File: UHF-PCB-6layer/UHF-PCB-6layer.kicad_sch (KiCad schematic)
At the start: 21 parts, among them IC1 MC100EL1648DG, U1 MAC-24+, U2 LTC1566-1IS8-PBF, U3 TAV1-331+, U5 XMSM0G3507SPT, U6 XC7A100T-CSG324_A

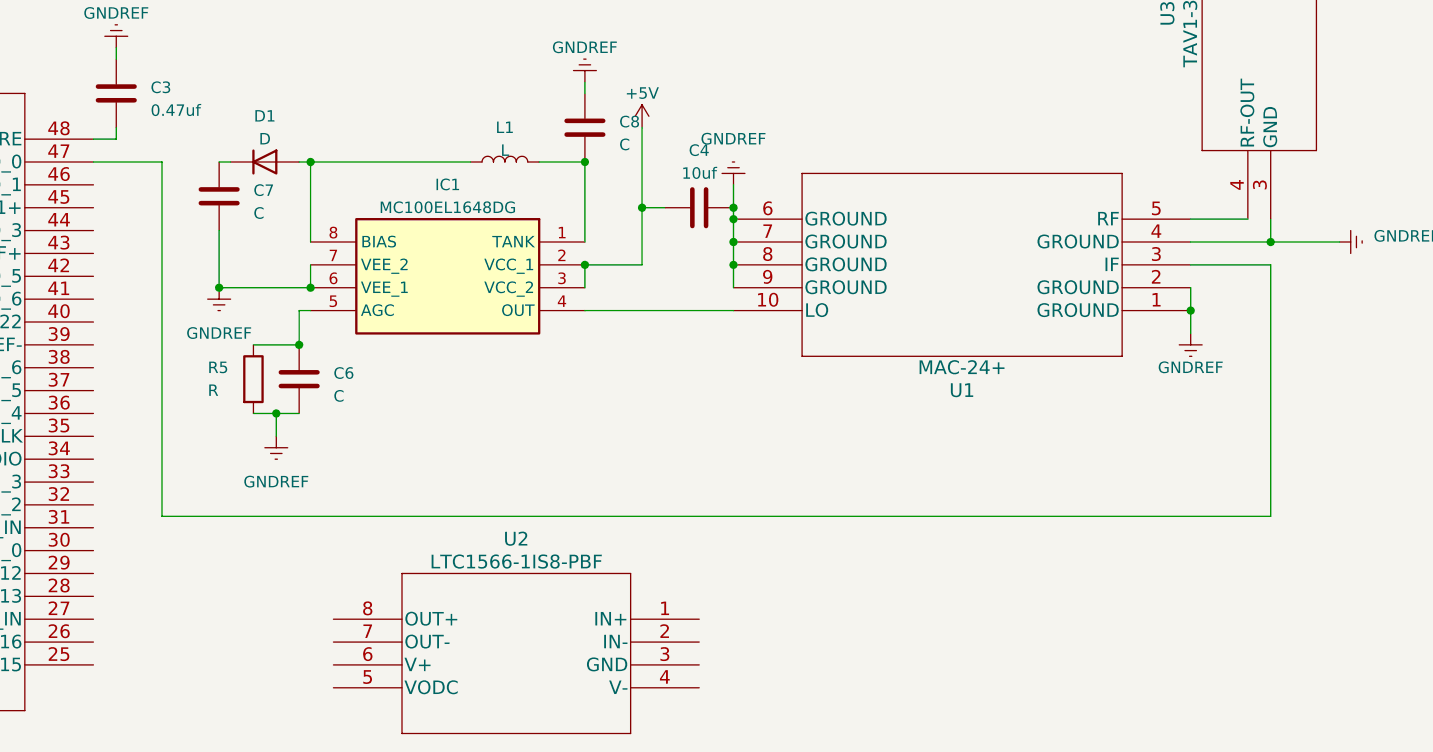
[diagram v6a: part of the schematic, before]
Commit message: added 2.3MHz LPF to input of module
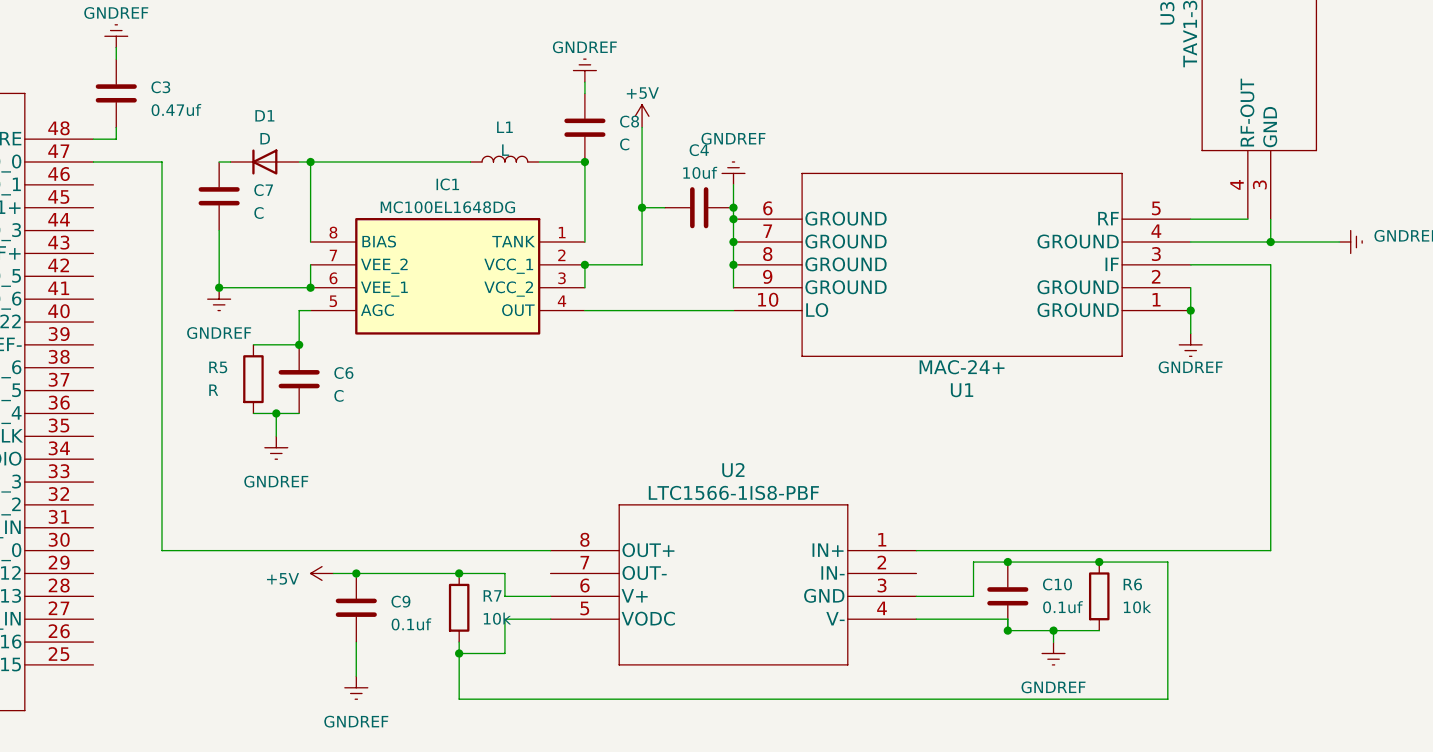
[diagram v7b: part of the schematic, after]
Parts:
- added C10, C9: 0.1uf, Capacitor_SMD:C_0603_1608Metric, symbol Device:C
- added R6, R7: 10k, Resistor_SMD:R_0603_1608Metric, symbol Device:R
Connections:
- net +5V: now also U2.6 (V+), C9.1, R7.1
- net GNDREF: now also U2.4 (V-), C10.2, C9.2, R6.2
- net at U1.3 (IF): now also U2.1 (IN+); no longer U5.47 (PA27_/_RTC_OUT_/_A0_0)
- net at U2.3 (GND): now also U2.5 (VODC), C10.1, R6.1, R7.2
- net at U2.8 (OUT+): now also U5.47 (PA27_/_RTC_OUT_/_A0_0)
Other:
- moved on the sheet: U2

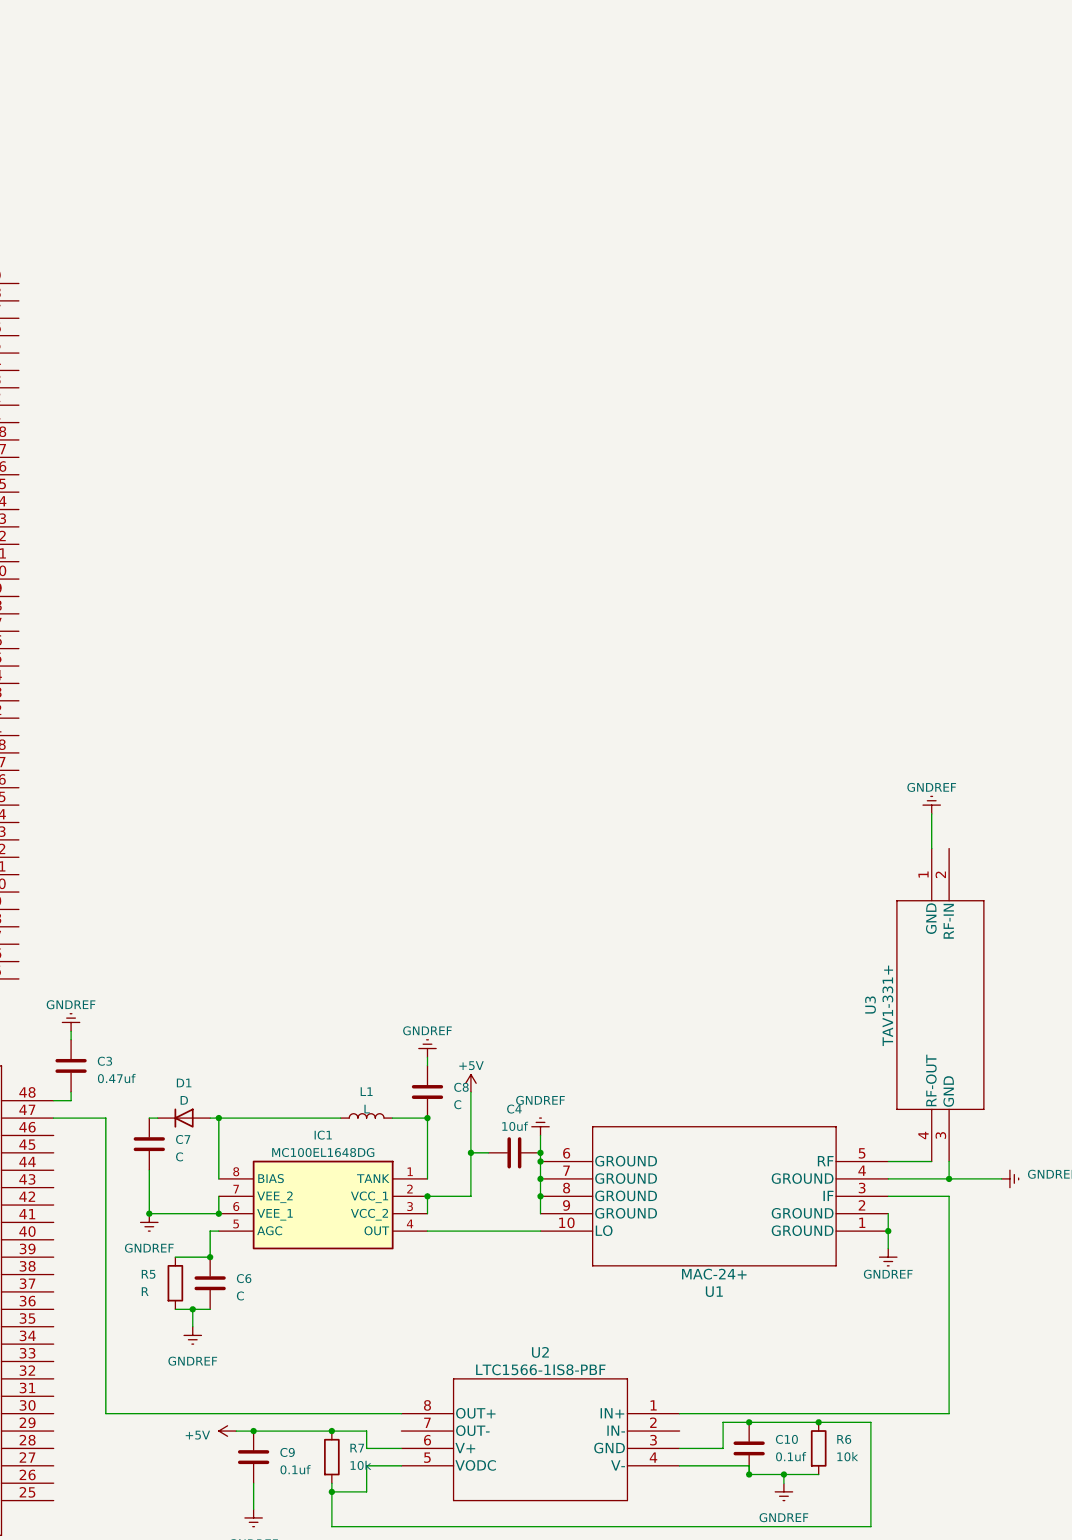
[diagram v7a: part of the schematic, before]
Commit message: added connector for power, 3.3v, 5v, gnd, and IF signal
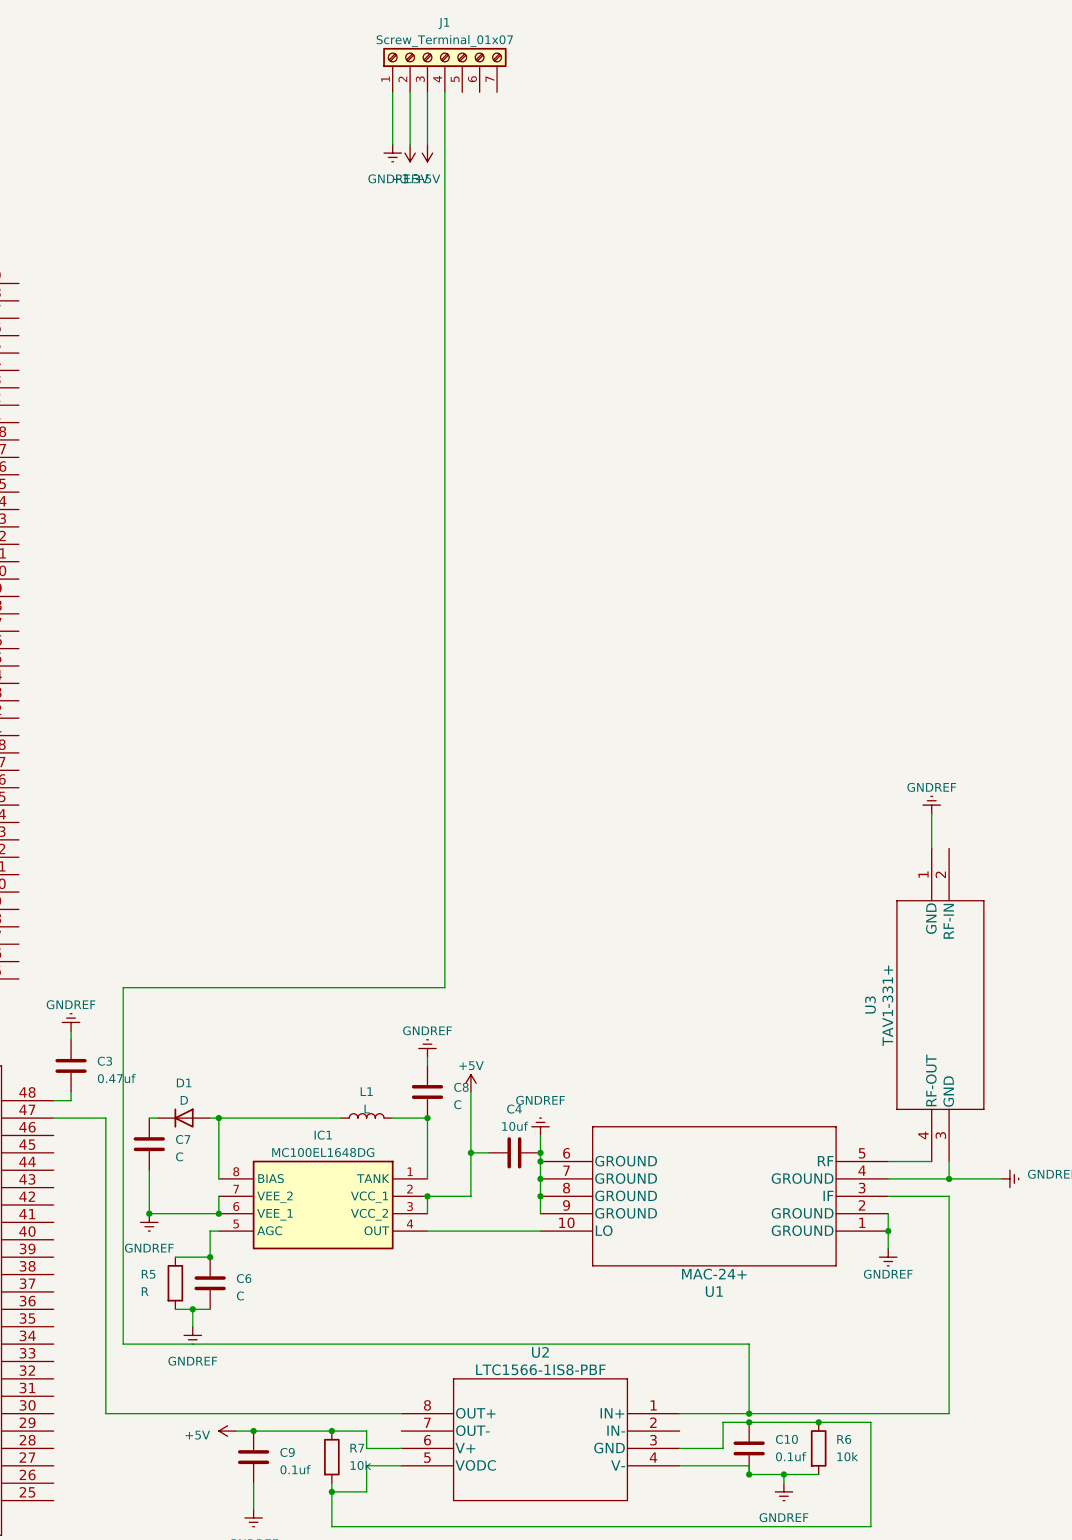
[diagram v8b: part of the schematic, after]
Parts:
- added J1: Screw_Terminal_01x07, TerminalBlock_Altech:Altech_AK300_1x07_P5.00mm_45-Degree, symbol Connector:Screw_Terminal_01x07
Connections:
- net +3.3V: now also J1.2 (Pin_2)
- net +5V: now also J1.3 (Pin_3)
- net GNDREF: now also J1.1 (Pin_1)
- net at U1.3 (IF), U2.1 (IN+): now also J1.4 (Pin_4)
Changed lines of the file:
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@@
   (junction (at 101.6 189.23) (diameter 0) (color 0 0 0 0)
   )
+  (junction (at 346.71 217.17) (diameter 0) (color 0 0 0 0)
+  )
   (junction (at 375.92 182.88) (diameter 0) (color 0 0 0 0)
   )
@@
     (stroke (width 0) (type default))
   )
+  (wire (pts (xy 302.26 154.94) (xy 255.27 154.94))
+    (stroke (width 0) (type default))
+  )
   (wire (pts (xy 101.6 193.04) (xy 101.6 195.58))
     (stroke (width 0) (type default))
@@
     (stroke (width 0) (type default))
   )
+  (wire (pts (xy 346.71 207.01) (xy 346.71 217.17))
+    (stroke (width 0) (type default))
+  )
   (wire (pts (xy 383.54 182.88) (xy 375.92 182.88))
     (stroke (width 0) (type default))
@@
     (stroke (width 0) (type default))
   )
+  (wire (pts (xy 299.72 24.13) (xy 299.72 31.75))
+    (stroke (width 0) (type default))
+  )
   (wire (pts (xy 308.61 179.07) (xy 306.07 179.07))
     (stroke (width 0) (type default))
@@
     (stroke (width 0) (type default))
   )
-  (wire (pts (xy 336.55 217.17) (xy 375.92 217.17))
+  (wire (pts (xy 336.55 217.17) (xy 346.71 217.17))
     (stroke (width 0) (type default))
   )
@@
     (stroke (width 0) (type default))
   )
+  (wire (pts (xy 294.64 24.13) (xy 294.64 31.75))
+    (stroke (width 0) (type default))
+  )
   (wire (pts (xy 364.49 218.44) (xy 364.49 233.68))
     (stroke (width 0) (type default))
@@
     (stroke (width 0) (type default))
   )
+  (wire (pts (xy 255.27 207.01) (xy 346.71 207.01))
+    (stroke (width 0) (type default))
+  )
+  (wire (pts (xy 255.27 154.94) (xy 255.27 207.01))
+    (stroke (width 0) (type default))
+  )
   (wire (pts (xy 118.11 173.99) (xy 123.19 173.99))
     (stroke (width 0) (type default))
   )
+  (wire (pts (xy 302.26 24.13) (xy 302.26 154.94))
+    (stroke (width 0) (type default))
+  )
   (wire (pts (xy 259.08 181.61) (xy 259.08 187.96))
     (stroke (width 0) (type default))
@@
     (stroke (width 0) (type default))
   )
+  (wire (pts (xy 346.71 217.17) (xy 375.92 217.17))
+    (stroke (width 0) (type default))
+  )
   (wire (pts (xy 123.19 173.99) (xy 123.19 167.64))
     (stroke (width 0) (type default))
@@
     (stroke (width 0) (type default))
   )
+  (wire (pts (xy 297.18 24.13) (xy 297.18 31.75))
+    (stroke (width 0) (type default))
+  )
   (wire (pts (xy 295.91 224.79) (xy 290.83 224.79))
     (stroke (width 0) (type default))
@@
         (path "/408f5dbf-8c57-4b84-b0cc-1d788fcf6d08"
           (reference "L1") (unit 1)
+        )
+      )
+    )
+  )
+  (symbol (lib_id "Connector:Screw_Terminal_01x07") (at 302.26 19.05 90) (unit 1)
+    (in_bom yes) (on_board yes) (dnp no) (fields_autoplaced)
+    (property "Reference" "J1" (at 302.26 13.97 90)
+      (effects (font (size 1.27 1.27)))
+    )
+    (property "Value" "Screw_Terminal_01x07" (at 302.26 16.51 90)
+      (effects (font (size 1.27 1.27)))
+    )
+    (property "Footprint" "TerminalBlock_Altech:Altech_AK300_1x07_P5.00mm_45-Degree" (at 302.26 19.05 0)
+      (effects (font (size 1.27 1.27)) hide)
+    )
+    (property "Datasheet" "~" (at 302.26 19.05 0)
+      (effects (font (size 1.27 1.27)) hide)
+    )
+    (pin "1")
+    (pin "2")
+    (pin "3")
+    (pin "4")
+    (pin "5")
+    (pin "6")
+    (pin "7")
+    (instances
+      (project "UHF-PCB-6layer"
+        (path "/408f5dbf-8c57-4b84-b0cc-1d788fcf6d08"
+          (reference "J1") (unit 1)
         )
       )
@@
         (path "/408f5dbf-8c57-4b84-b0cc-1d788fcf6d08"
           (reference "U1") (unit 1)
+        )
+      )
+    )
+  )
+  (symbol (lib_id "power:+5V") (at 299.72 31.75 180) (unit 1)
+    (in_bom yes) (on_board yes) (dnp no) (fields_autoplaced)
+    (property "Reference" "#PWR018" (at 299.72 27.94 0)
+      (effects (font (size 1.27 1.27)) hide)
+    )
+    (property "Value" "+5V" (at 299.72 36.83 0)
+      (effects (font (size 1.27 1.27)))
+    )
+    (property "Footprint" "" (at 299.72 31.75 0)
+      (effects (font (size 1.27 1.27)) hide)
+    )
+    (property "Datasheet" "" (at 299.72 31.75 0)
+      (effects (font (size 1.27 1.27)) hide)
+    )
+    (pin "1")
+    (instances
+      (project "UHF-PCB-6layer"
+        (path "/408f5dbf-8c57-4b84-b0cc-1d788fcf6d08"
+          (reference "#PWR018") (unit 1)
         )
       )
@@
         )
       )
+    )
+  )
+  (symbol (lib_id "power:GNDREF") (at 294.64 31.75 0) (unit 1)
+    (in_bom yes) (on_board yes) (dnp no) (fields_autoplaced)
+    (property "Reference" "#PWR017" (at 294.64 38.1 0)
+      (effects (font (size 1.27 1.27)) hide)
+    )
+    (property "Value" "GNDREF" (at 294.64 36.83 0)
+      (effects (font (size 1.27 1.27)))
+    )
+    (property "Footprint" "" (at 294.64 31.75 0)
+      (effects (font (size 1.27 1.27)) hide)
+    )
+    (property "Datasheet" "" (at 294.64 31.75 0)
+      (effects (font (size 1.27 1.27)) hide)
+    )
+    (pin "1")
+    (instances
+      (project "UHF-PCB-6layer"
+        (path "/408f5dbf-8c57-4b84-b0cc-1d788fcf6d08"
+          (reference "#PWR017") (unit 1)
+        )
+      )
+    )
+  )
+  (symbol (lib_id "power:+3.3V") (at 297.18 31.75 180) (unit 1)
+    (in_bom yes) (on_board yes) (dnp no) (fields_autoplaced)
+    (property "Reference" "#PWR019" (at 297.18 27.94 0)
+      (effects (font (size 1.27 1.27)) hide)
+    )
+    (property "Value" "+3.3V" (at 297.18 36.83 0)
+      (effects (font (size 1.27 1.27)))
+    )
+    (property "Footprint" "" (at 297.18 31.75 0)
+      (effects (font (size 1.27 1.27)) hide)
+    )
+    (property "Datasheet" "" (at 297.18 31.75 0)
+      (effects (font (size 1.27 1.27)) hide)
+    )
+    (pin "1")
+    (instances
+      (project "UHF-PCB-6layer"
+        (path "/408f5dbf-8c57-4b84-b0cc-1d788fcf6d08"
+          (reference "#PWR019") (unit 1)
+        )
+      )
